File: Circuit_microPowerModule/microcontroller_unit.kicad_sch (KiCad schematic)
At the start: 23 parts, among them J1 USB_C_Receptacle_USB2.0, SW2 KMR2, SW3 KMR2, U6 RP2040, U9 W25Q128JVS, Y1 12MHz

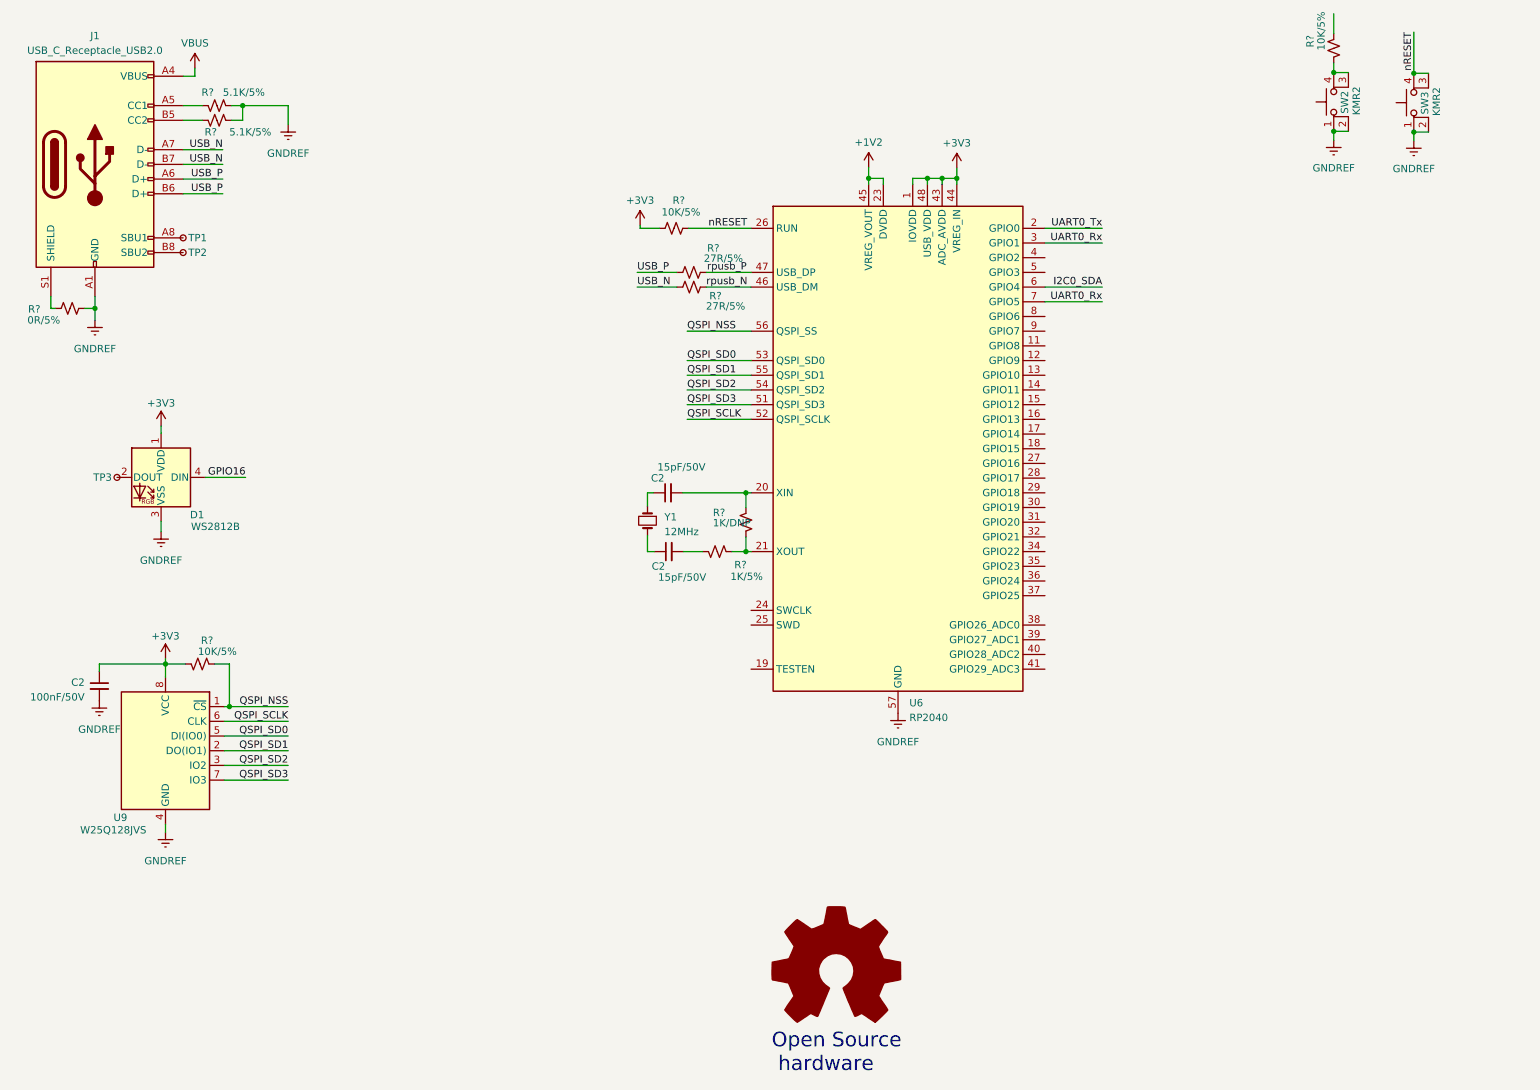
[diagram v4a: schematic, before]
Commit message: added mikrobus header
added filter capacitance, I2C pull-up resistor
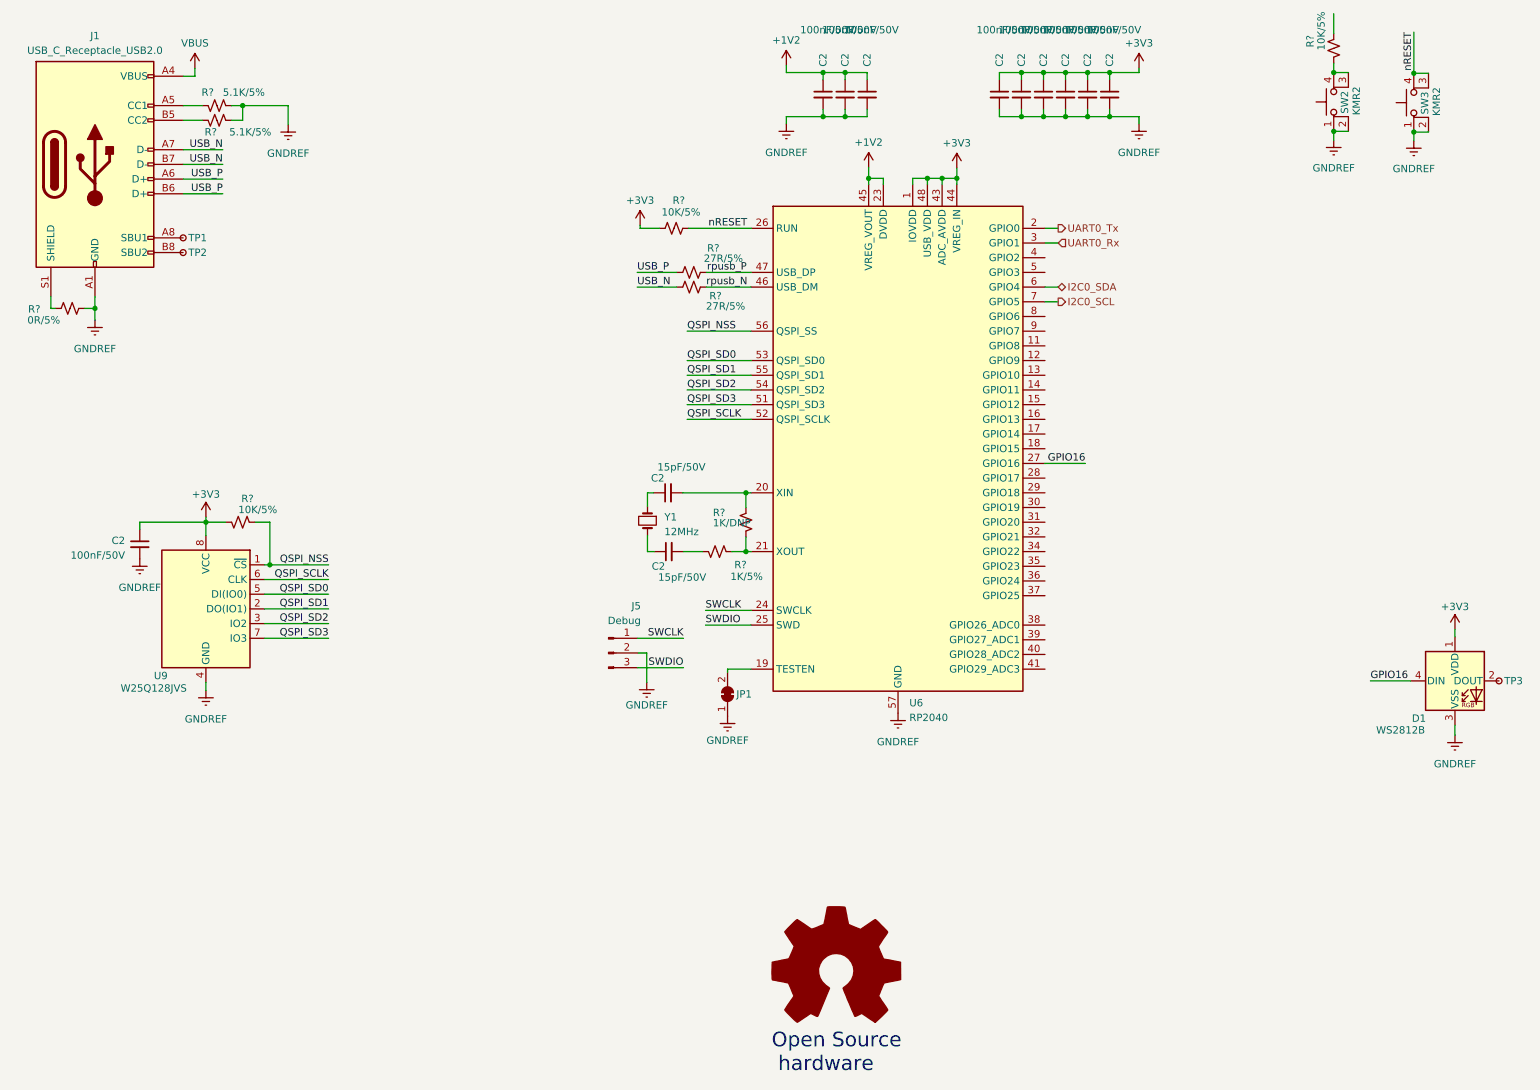
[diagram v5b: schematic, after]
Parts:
- added C2 (x9): 100nF/50V, symbol Device:C_Small
- added J5: Debug, symbol Connector:Conn_01x03_Pin
- added JP1: SolderJumper_2_Bridged, symbol Jumper:SolderJumper_2_Bridged
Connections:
- net +1V2: now also C2.1, C2.1, C2.1
- net +3V3: now also C2.1, C2.1, C2.1, C2.1, C2.1, C2.1
- net GNDREF: now also C2.2, C2.2, C2.2, C2.2, C2.2, C2.2, C2.2, C2.2, C2.2, J5.2 (Pin_2), JP1.1 (A)
- net GPIO16: now also U6.27 (GPIO16)
- net UART0_Rx: no longer U6.7 (GPIO5)
- net at U6.19 (TESTEN): now also JP1.2 (B)
- net SWCLK: now reaches U6.24 (SWCLK)
- net SWCLK: now also J5.1 (Pin_1)
- net SWDIO: now reaches U6.25 (SWD)
- net SWDIO: now also J5.3 (Pin_3)
- new net I2C0_SCL: U6.7 (GPIO5)
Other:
- moved on the sheet: C2, D1, R?, TP3, U9

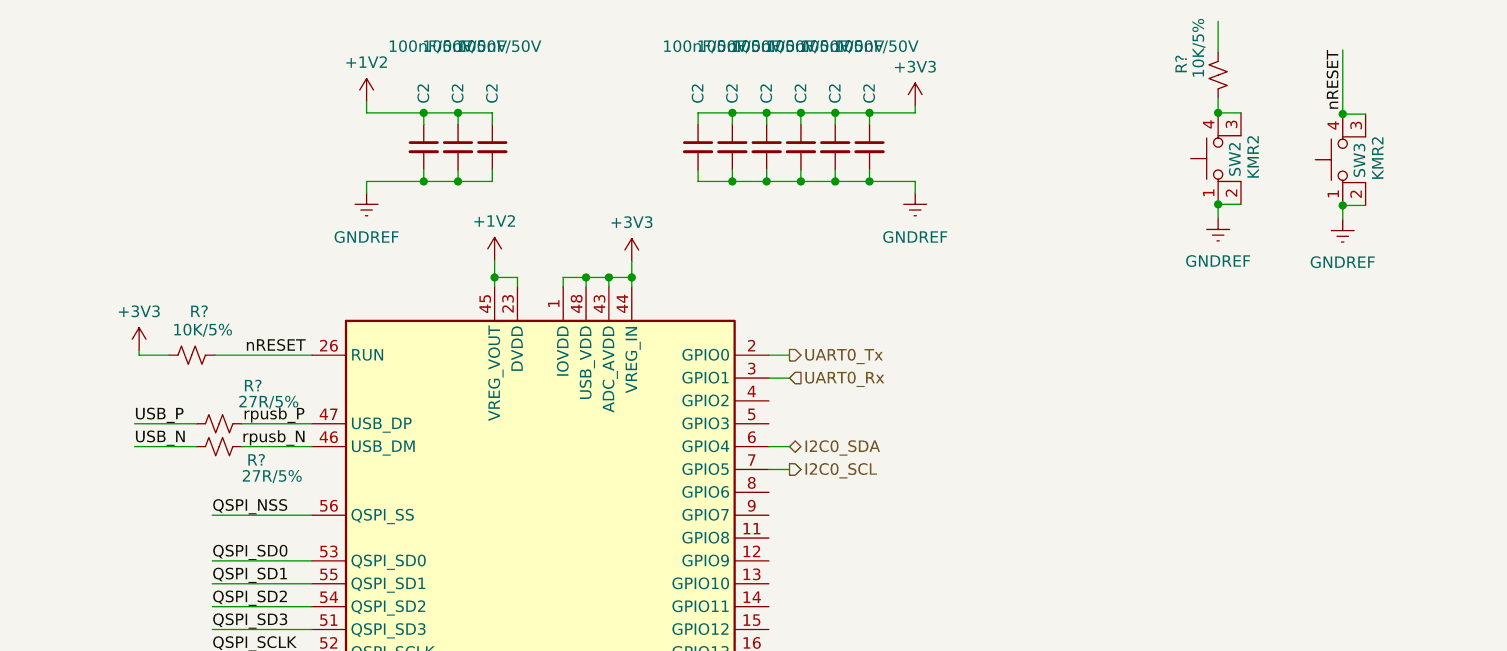
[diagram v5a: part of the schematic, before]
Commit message: added Nokia 5110 LCD symbol
linked some component pin
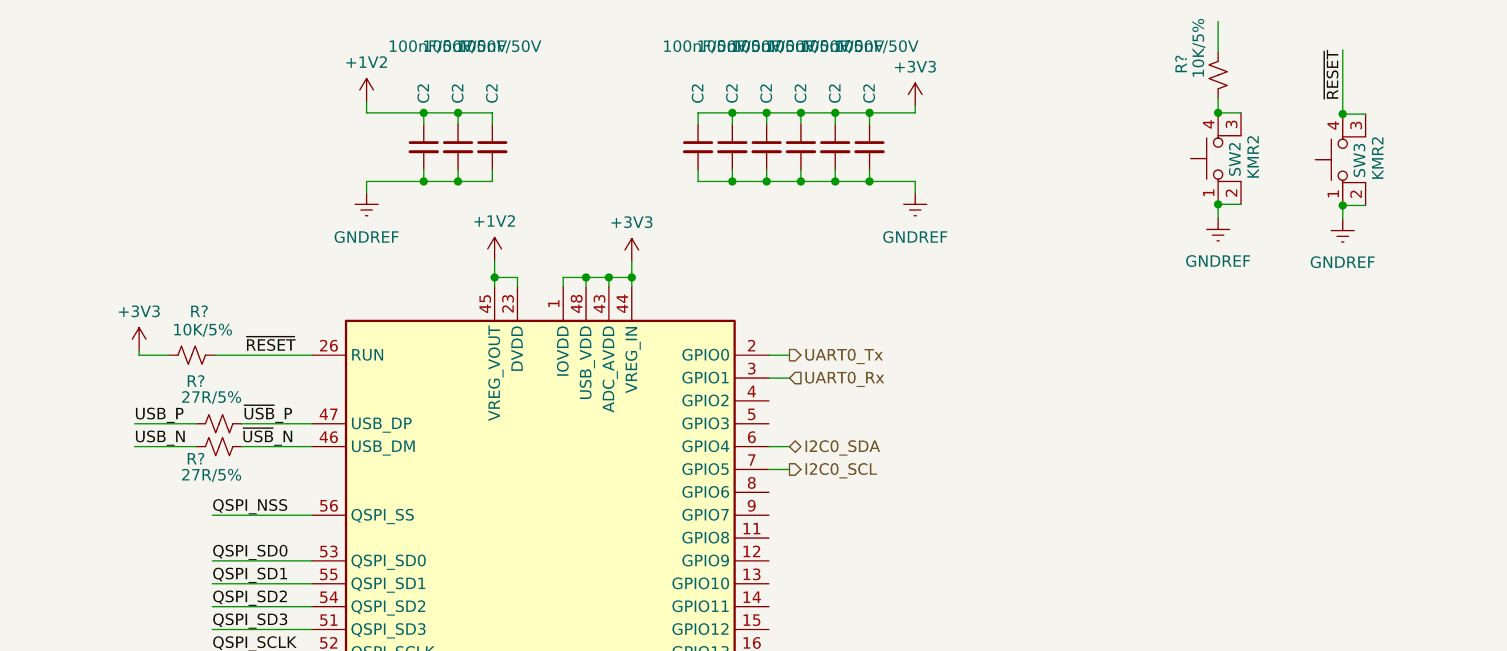
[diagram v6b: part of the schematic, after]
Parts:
- J1: footprint (none) -> Connector_USB:USB_C_Receptacle_G-Switch_GT-USB-7010ASV
- JP1: footprint (none) -> Jumper:SolderJumper-2_P1.3mm_Bridged_Pad1.0x1.5mm
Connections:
- net nRESET renamed ~{RESET}
- net rpusb_N renamed ~{USB}_N
- net rpusb_P renamed ~{USB}_P
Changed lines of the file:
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@@
     (effects (font (size 1.27 1.27)) (justify left bottom))
   )
-  (label "rpusb_P" (at 137.414 58.674 0) (fields_autoplaced)
+  (label "~{USB}_P" (at 137.414 58.674 0) (fields_autoplaced)
     (effects (font (size 1.27 1.27)) (justify left bottom))
   )
@@
     (effects (font (size 1.27 1.27)) (justify right bottom))
   )
-  (label "rpusb_N" (at 137.287 61.214 0) (fields_autoplaced)
+  (label "~{USB}_N" (at 137.287 61.214 0) (fields_autoplaced)
     (effects (font (size 1.27 1.27)) (justify left bottom))
   )
@@
     (effects (font (size 1.27 1.27)) (justify right bottom))
   )
-  (label "nRESET" (at 137.668 51.054 0) (fields_autoplaced)
+  (label "~{RESET}" (at 137.668 51.054 0) (fields_autoplaced)
     (effects (font (size 1.27 1.27)) (justify left bottom))
   )
@@
     (effects (font (size 1.27 1.27)) (justify left bottom))
   )
-  (label "nRESET" (at 259.588 17.145 270) (fields_autoplaced)
+  (label "~{RESET}" (at 259.588 17.145 270) (fields_autoplaced)
     (effects (font (size 1.27 1.27)) (justify right bottom))
   )
@@
   (symbol (lib_id "Device:R_Small_US") (at 134.747 58.674 270) (unit 1)
     (in_bom yes) (on_board yes) (dnp no)
-    (property "Reference" "R?" (at 139.573 54.483 90)
-      (effects (font (size 1.27 1.27)) (justify right))
-    )
-    (property "Value" "27R/5%" (at 143.637 56.261 90)
+    (property "Reference" "R?" (at 133.223 53.975 90)
+      (effects (font (size 1.27 1.27)) (justify right))
+    )
+    (property "Value" "27R/5%" (at 137.287 55.753 90)
       (effects (font (size 1.27 1.27)) (justify right))
     )
@@
   (symbol (lib_id "Device:R_Small_US") (at 134.747 61.214 270) (unit 1)
     (in_bom yes) (on_board yes) (dnp no)
-    (property "Reference" "R?" (at 139.954 62.738 90)
-      (effects (font (size 1.27 1.27)) (justify right))
-    )
-    (property "Value" "27R/5%" (at 144.018 64.516 90)
+    (property "Reference" "R?" (at 133.223 62.611 90)
+      (effects (font (size 1.27 1.27)) (justify right))
+    )
+    (property "Value" "27R/5%" (at 137.287 64.389 90)
       (effects (font (size 1.27 1.27)) (justify right))
     )
@@
       (effects (font (size 1.27 1.27)) (justify right) hide)
     )
-    (property "Footprint" "" (at 140.97 131.572 0)
+    (property "Footprint" "Jumper:SolderJumper-2_P1.3mm_Bridged_Pad1.0x1.5mm" (at 140.97 131.572 0)
       (effects (font (size 1.27 1.27)) hide)
     )
@@
       (effects (font (size 1.27 1.27)))
     )
-    (property "Footprint" "" (at 35.433 40.005 0)
-      (effects (font (size 1.27 1.27)) hide)
-    )
+    (property "Footprint" "Connector_USB:USB_C_Receptacle_G-Switch_GT-USB-7010ASV" (at 35.433 40.005 0)
+      (effects (font (size 1.27 1.27)) hide)
+    )

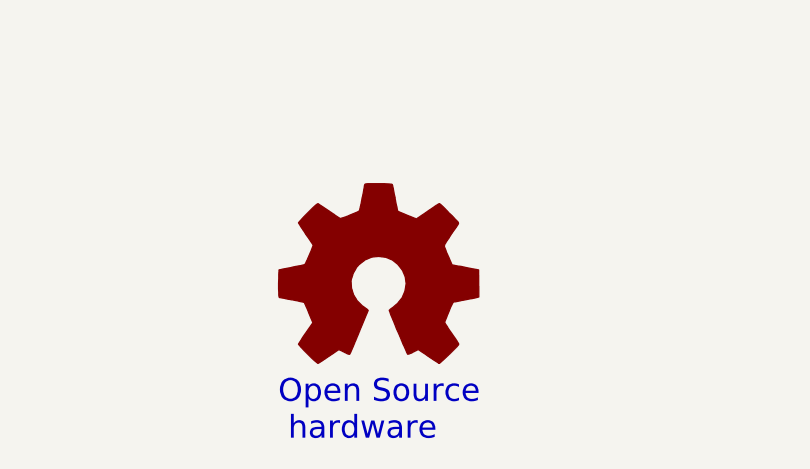
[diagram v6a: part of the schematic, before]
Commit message: added schematic svg file
added encoder wire, mikrobus connect
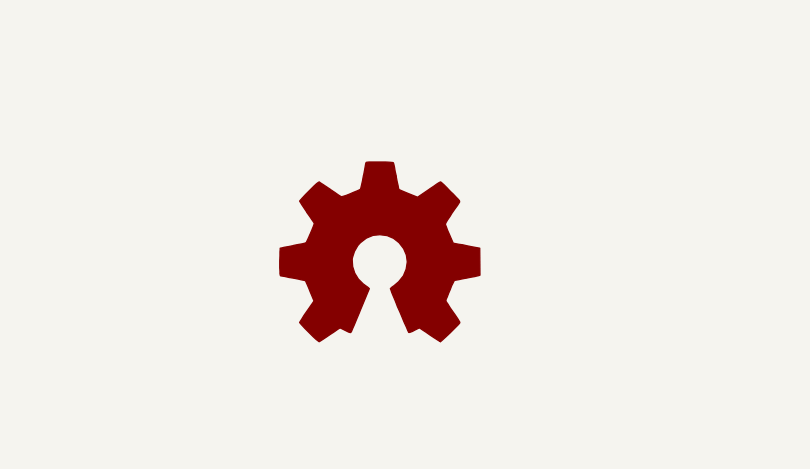
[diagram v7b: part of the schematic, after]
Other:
- note removed: "Open Source hardware"
